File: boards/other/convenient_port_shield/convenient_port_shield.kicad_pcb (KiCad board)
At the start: 2 copper layers, 54.6 x 55.9 mm, 7 parts, among them J1 Conn_01x08, J2 Conn_01x06, J3 Conn_01x08, J4 Conn_01x10, J5 Conn_02x06_Top_Bottom, J6 Conn_02x06_Top_Bottom, J7 VCC_select

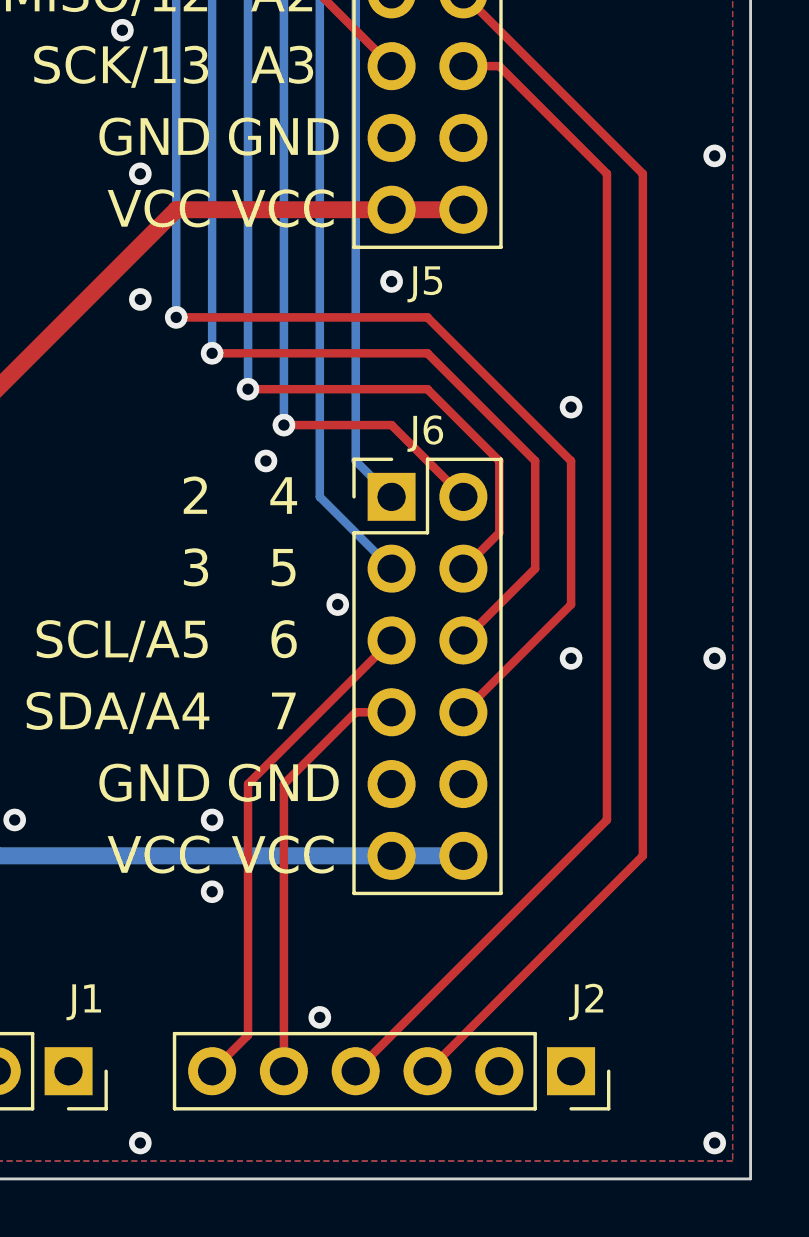
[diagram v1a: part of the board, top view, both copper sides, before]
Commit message: fix rom_write_shield and convenient_port_shield
fix reversed Arduino analog ports
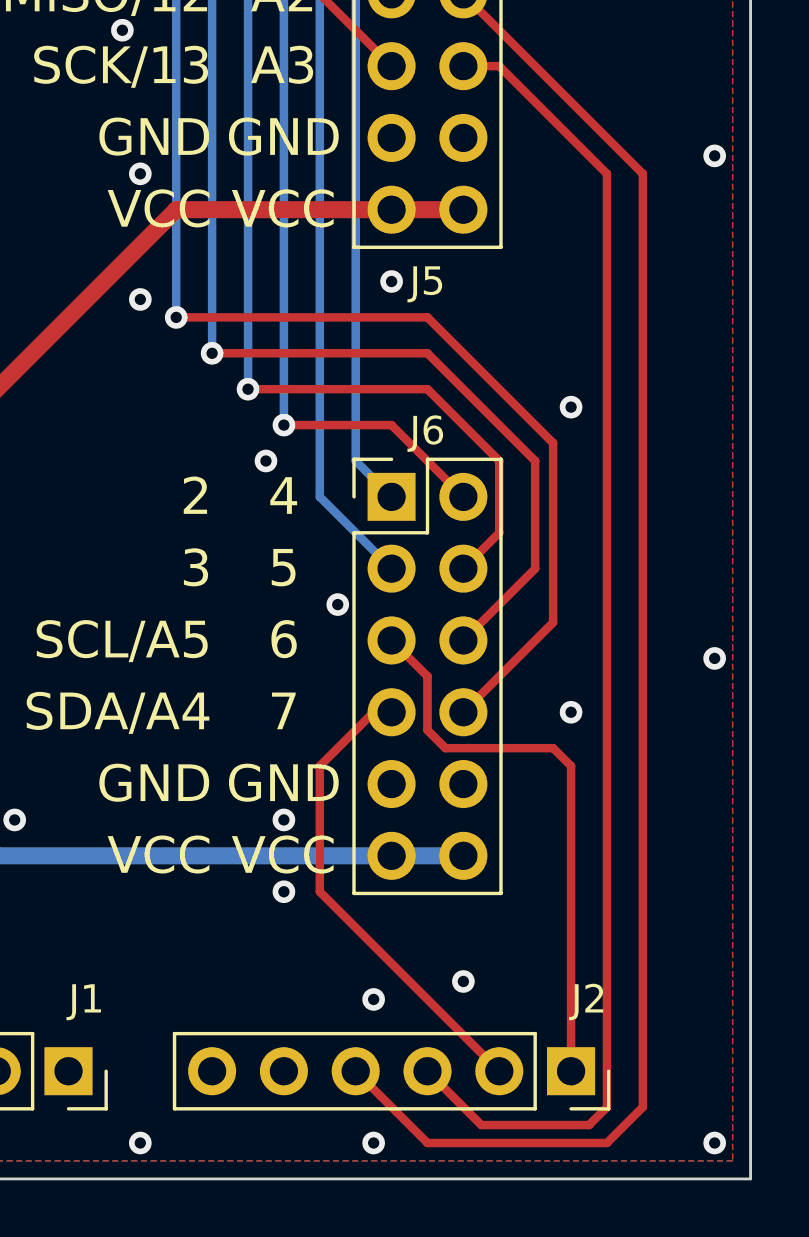
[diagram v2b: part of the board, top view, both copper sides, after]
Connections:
- J2 pad 1: unconnected-(J2-Pad1) -> /SCL
- J2 pad 2: unconnected-(J2-Pad2) -> /SDA
- J2 pad 3: /A2 -> /A3
- J2 pad 4: /A3 -> /A2
- J2 pad 5: /SDA -> unconnected-(J2-Pad5)
- J2 pad 6: /SCL -> unconnected-(J2-Pad6)
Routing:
- net /A2: track 43.9 -> 53.7 mm
- net /A3: track 42.1 -> 47.1 mm
- net /SCL: track 17.9 -> 20.1 mm
- net /SDA: track 15.0 -> 16.8 mm
- net /D7: track 49.7 -> 49.2 mm
- net GND: vias 29 -> 31
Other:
- board text added: "Convenient Port Shield v1.1"
- board text removed: "Convenient Port Shield v1.0"
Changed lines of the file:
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@@
   (net 6 "/IOREF")
   (net 7 "unconnected-(J1-Pad8)")
-  (net 8 "unconnected-(J2-Pad1)")
-  (net 9 "unconnected-(J2-Pad2)")
+  (net 8 "unconnected-(J2-Pad5)")
+  (net 9 "unconnected-(J2-Pad6)")
   (net 10 "/A2")
   (net 11 "/A3")
@@
     (fp_line (start 1.27 13.97) (end -1.27 13.97) (layer "F.Fab") (width 0.1))
     (pad "1" thru_hole rect (at 0 0 270) (size 1.7 1.7) (drill 1) (layers *.Cu *.Mask)
-      (net 8 "unconnected-(J2-Pad1)") (pinfunction "Pin_1") (pintype "passive+no_connect"))
+      (net 13 "/SCL") (pinfunction "Pin_1") (pintype "passive"))
     (pad "2" thru_hole oval (at 0 2.54 270) (size 1.7 1.7) (drill 1) (layers *.Cu *.Mask)
-      (net 9 "unconnected-(J2-Pad2)") (pinfunction "Pin_2") (pintype "passive+no_connect"))
+      (net 12 "/SDA") (pinfunction "Pin_2") (pintype "passive"))
     (pad "3" thru_hole oval (at 0 5.08 270) (size 1.7 1.7) (drill 1) (layers *.Cu *.Mask)
-      (net 10 "/A2") (pinfunction "Pin_3") (pintype "passive"))
+      (net 11 "/A3") (pinfunction "Pin_3") (pintype "passive"))
     (pad "4" thru_hole oval (at 0 7.62 270) (size 1.7 1.7) (drill 1) (layers *.Cu *.Mask)
-      (net 11 "/A3") (pinfunction "Pin_4") (pintype "passive"))
+      (net 10 "/A2") (pinfunction "Pin_4") (pintype "passive"))
     (pad "5" thru_hole oval (at 0 10.16 270) (size 1.7 1.7) (drill 1) (layers *.Cu *.Mask)
-      (net 12 "/SDA") (pinfunction "Pin_5") (pintype "passive"))
+      (net 8 "unconnected-(J2-Pad5)") (pinfunction "Pin_5") (pintype "passive+no_connect"))
     (pad "6" thru_hole oval (at 0 12.7 270) (size 1.7 1.7) (drill 1) (layers *.Cu *.Mask)
-      (net 13 "/SCL") (pinfunction "Pin_6") (pintype "passive"))
+      (net 9 "unconnected-(J2-Pad6)") (pinfunction "Pin_6") (pintype "passive+no_connect"))
     (model "${KICAD6_3DMODEL_DIR}/Connector_PinSocket_2.54mm.3dshapes/PinSocket_1x06_P2.54mm_Vertical.wrl"
       (offset (xyz 0 0 0))
@@
   )
   (gr_rect (start 135.89 39.37) (end 190.5 95.25) (layer "Edge.Cuts") (width 0.1) (fill none))
-  (gr_text "Convenient Port Shield\nv1.0" (at 172.085 69.85) (layer "B.SilkS")
+  (gr_text "Convenient Port Shield\nv1.1" (at 172.085 69.85) (layer "B.SilkS")
     (effects (font (size 2 2) (thickness 0.3)) (justify left mirror))
   )
@@
   )
   (via (at 150.495 59.055) (size 0.8) (drill 0.4) (layers "F.Cu" "B.Cu") (free) (net 2))
-  (via (at 171.45 82.55) (size 0.8) (drill 0.4) (layers "F.Cu" "B.Cu") (free) (net 2))
+  (via (at 173.99 82.55) (size 0.8) (drill 0.4) (layers "F.Cu" "B.Cu") (free) (net 2))
   (via (at 158.75 73.66) (size 0.8) (drill 0.4) (layers "F.Cu" "B.Cu") (free) (net 2))
   (via (at 189.23 76.835) (size 0.8) (drill 0.4) (layers "F.Cu" "B.Cu") (free) (net 2))
@@
   (via (at 152.4 88.265) (size 0.8) (drill 0.4) (layers "F.Cu" "B.Cu") (free) (net 2))
   (via (at 189.23 93.98) (size 0.8) (drill 0.4) (layers "F.Cu" "B.Cu") (free) (net 2))
-  (via (at 184.15 76.835) (size 0.8) (drill 0.4) (layers "F.Cu" "B.Cu") (free) (net 2))
-  (via (at 175.26 89.535) (size 0.8) (drill 0.4) (layers "F.Cu" "B.Cu") (free) (net 2))
+  (via (at 184.15 78.74) (size 0.8) (drill 0.4) (layers "F.Cu" "B.Cu") (free) (net 2))
+  (via (at 177.165 88.9) (size 0.8) (drill 0.4) (layers "F.Cu" "B.Cu") (free) (net 2))
   (via (at 150.495 76.835) (size 0.8) (drill 0.4) (layers "F.Cu" "B.Cu") (free) (net 2))
-  (via (at 171.45 85.09) (size 0.8) (drill 0.4) (layers "F.Cu" "B.Cu") (free) (net 2))
+  (via (at 173.99 85.09) (size 0.8) (drill 0.4) (layers "F.Cu" "B.Cu") (free) (net 2))
   (via (at 175.895 74.93) (size 0.8) (drill 0.4) (layers "F.Cu" "B.Cu") (free) (net 2))
   (via (at 168.91 64.135) (size 0.8) (drill 0.4) (layers "F.Cu" "B.Cu") (free) (net 2))
   (via (at 137.16 40.64) (size 0.8) (drill 0.4) (layers "F.Cu" "B.Cu") (free) (net 2))
   (via (at 137.16 76.835) (size 0.8) (drill 0.4) (layers "F.Cu" "B.Cu") (free) (net 2))
+  (via (at 180.34 88.265) (size 0.8) (drill 0.4) (layers "F.Cu" "B.Cu") (free) (net 2))
   (via (at 137.16 93.98) (size 0.8) (drill 0.4) (layers "F.Cu" "B.Cu") (free) (net 2))
+  (via (at 177.165 93.98) (size 0.8) (drill 0.4) (layers "F.Cu" "B.Cu") (free) (net 2))
   (via (at 189.23 59.055) (size 0.8) (drill 0.4) (layers "F.Cu" "B.Cu") (free) (net 2))
   (via (at 184.15 67.945) (size 0.8) (drill 0.4) (layers "F.Cu" "B.Cu") (free) (net 2))
@@
   (segment (start 157.48 76.2) (end 158.75 76.2) (width 0.6) (layer "F.Cu") (net 6))
   (segment (start 153.67 80.01) (end 153.67 88.9) (width 0.6) (layer "F.Cu") (net 6))
+  (segment (start 179.07 93.98) (end 176.53 91.44) (width 0.3) (layer "F.Cu") (net 10))
+  (segment (start 186.69 59.69) (end 186.69 92.71) (width 0.3) (layer "F.Cu") (net 10))
+  (segment (start 185.42 93.98) (end 179.07 93.98) (width 0.3) (layer "F.Cu") (net 10))
+  (segment (start 186.69 92.71) (end 185.42 93.98) (width 0.3) (layer "F.Cu") (net 10))
   (segment (start 180.34 53.34) (end 186.69 59.69) (width 0.3) (layer "F.Cu") (net 10))
-  (segment (start 186.69 59.69) (end 186.69 83.82) (width 0.3) (layer "F.Cu") (net 10))
-  (segment (start 186.69 83.82) (end 179.07 91.44) (width 0.3) (layer "F.Cu") (net 10))
+  (segment (start 185.42 92.71) (end 184.785 93.345) (width 0.3) (layer "F.Cu") (net 11))
+  (segment (start 181.61 55.88) (end 185.42 59.69) (width 0.3) (layer "F.Cu") (net 11))
+  (segment (start 184.785 93.345) (end 180.975 93.345) (width 0.3) (layer "F.Cu") (net 11))
+  (segment (start 180.975 93.345) (end 179.07 91.44) (width 0.3) (layer "F.Cu") (net 11))
+  (segment (start 185.42 59.69) (end 185.42 92.71) (width 0.3) (layer "F.Cu") (net 11))
   (segment (start 180.34 55.88) (end 181.61 55.88) (width 0.3) (layer "F.Cu") (net 11))
-  (segment (start 181.61 55.88) (end 185.42 59.69) (width 0.3) (layer "F.Cu") (net 11))
-  (segment (start 185.42 59.69) (end 185.42 82.55) (width 0.3) (layer "F.Cu") (net 11))
-  (segment (start 185.42 82.55) (end 176.53 91.44) (width 0.3) (layer "F.Cu") (net 11))
-  (segment (start 173.99 81.28) (end 173.99 91.44) (width 0.3) (layer "F.Cu") (net 12))
-  (segment (start 176.53 78.74) (end 173.99 81.28) (width 0.3) (layer "F.Cu") (net 12))
-  (segment (start 177.8 78.74) (end 176.53 78.74) (width 0.3) (layer "F.Cu") (net 12))
-  (segment (start 172.72 90.17) (end 172.72 81.28) (width 0.3) (layer "F.Cu") (net 13))
-  (segment (start 171.45 91.44) (end 172.72 90.17) (width 0.3) (layer "F.Cu") (net 13))
-  (segment (start 172.72 81.28) (end 177.8 76.2) (width 0.3) (layer "F.Cu") (net 13))
+  (segment (start 175.26 80.645) (end 175.26 85.09) (width 0.3) (layer "F.Cu") (net 12))
+  (segment (start 175.26 85.09) (end 181.61 91.44) (width 0.3) (layer "F.Cu") (net 12))
+  (segment (start 177.8 78.74) (end 177.165 78.74) (width 0.3) (layer "F.Cu") (net 12))
+  (segment (start 177.165 78.74) (end 175.26 80.645) (width 0.3) (layer "F.Cu") (net 12))
+  (segment (start 177.8 76.2) (end 179.07 77.47) (width 0.3) (layer "F.Cu") (net 13))
+  (segment (start 184.15 80.645) (end 184.15 91.44) (width 0.3) (layer "F.Cu") (net 13))
+  (segment (start 183.515 80.01) (end 184.15 80.645) (width 0.3) (layer "F.Cu") (net 13))
+  (segment (start 179.07 77.47) (end 179.07 79.375) (width 0.3) (layer "F.Cu") (net 13))
+  (segment (start 179.07 79.375) (end 179.705 80.01) (width 0.3) (layer "F.Cu") (net 13))
+  (segment (start 179.705 80.01) (end 183.515 80.01) (width 0.3) (layer "F.Cu") (net 13))
   (segment (start 176.53 45.72) (end 176.53 69.85) (width 0.3) (layer "B.Cu") (net 16))
   (segment (start 179.07 43.18) (end 176.53 45.72) (width 0.3) (layer "B.Cu") (net 16))
@@
   (segment (start 168.91 43.18) (end 171.45 45.72) (width 0.3) (layer "B.Cu") (net 20))
   (segment (start 171.45 45.72) (end 171.45 66.04) (width 0.3) (layer "B.Cu") (net 20))
-  (segment (start 184.15 69.85) (end 184.15 74.93) (width 0.3) (layer "F.Cu") (net 21))
-  (segment (start 179.07 64.77) (end 184.15 69.85) (width 0.3) (layer "F.Cu") (net 21))
+  (segment (start 183.515 69.215) (end 183.515 75.565) (width 0.3) (layer "F.Cu") (net 21))
   (segment (start 170.18 64.77) (end 179.07 64.77) (width 0.3) (layer "F.Cu") (net 21))
-  (segment (start 184.15 74.93) (end 180.34 78.74) (width 0.3) (layer "F.Cu") (net 21))
+  (segment (start 183.515 75.565) (end 180.34 78.74) (width 0.3) (layer "F.Cu") (net 21))
+  (segment (start 179.07 64.77) (end 183.515 69.215) (width 0.3) (layer "F.Cu") (net 21))
   (via (at 170.18 64.77) (size 0.8) (drill 0.4) (layers "F.Cu" "B.Cu") (net 21))
   (segment (start 166.37 43.18) (end 170.18 46.99) (width 0.3) (layer "B.Cu") (net 21))
